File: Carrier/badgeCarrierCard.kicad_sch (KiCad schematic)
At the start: 29 parts, among them J1 USB_C_Receptacle_USB2.0_16P, J2 MDT420M02003, J3 Conn_01x08, J7 Conn_01x10, U11 TPSGM7227YUWQ10G

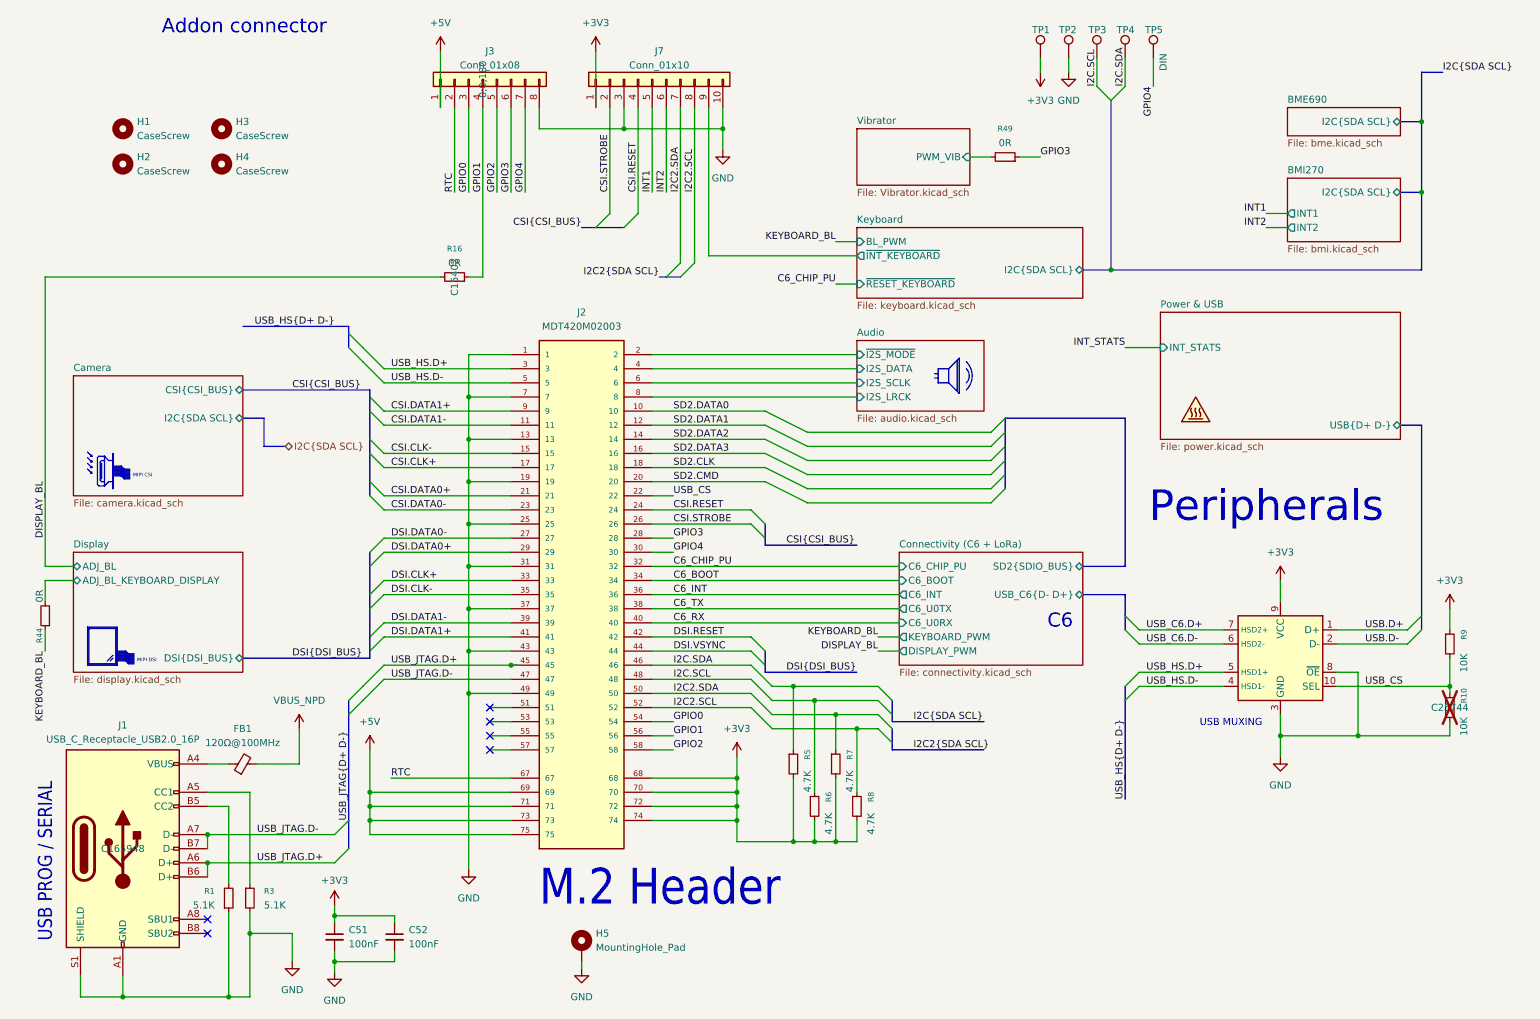
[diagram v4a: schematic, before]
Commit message: feat: add leds and 3dmodels
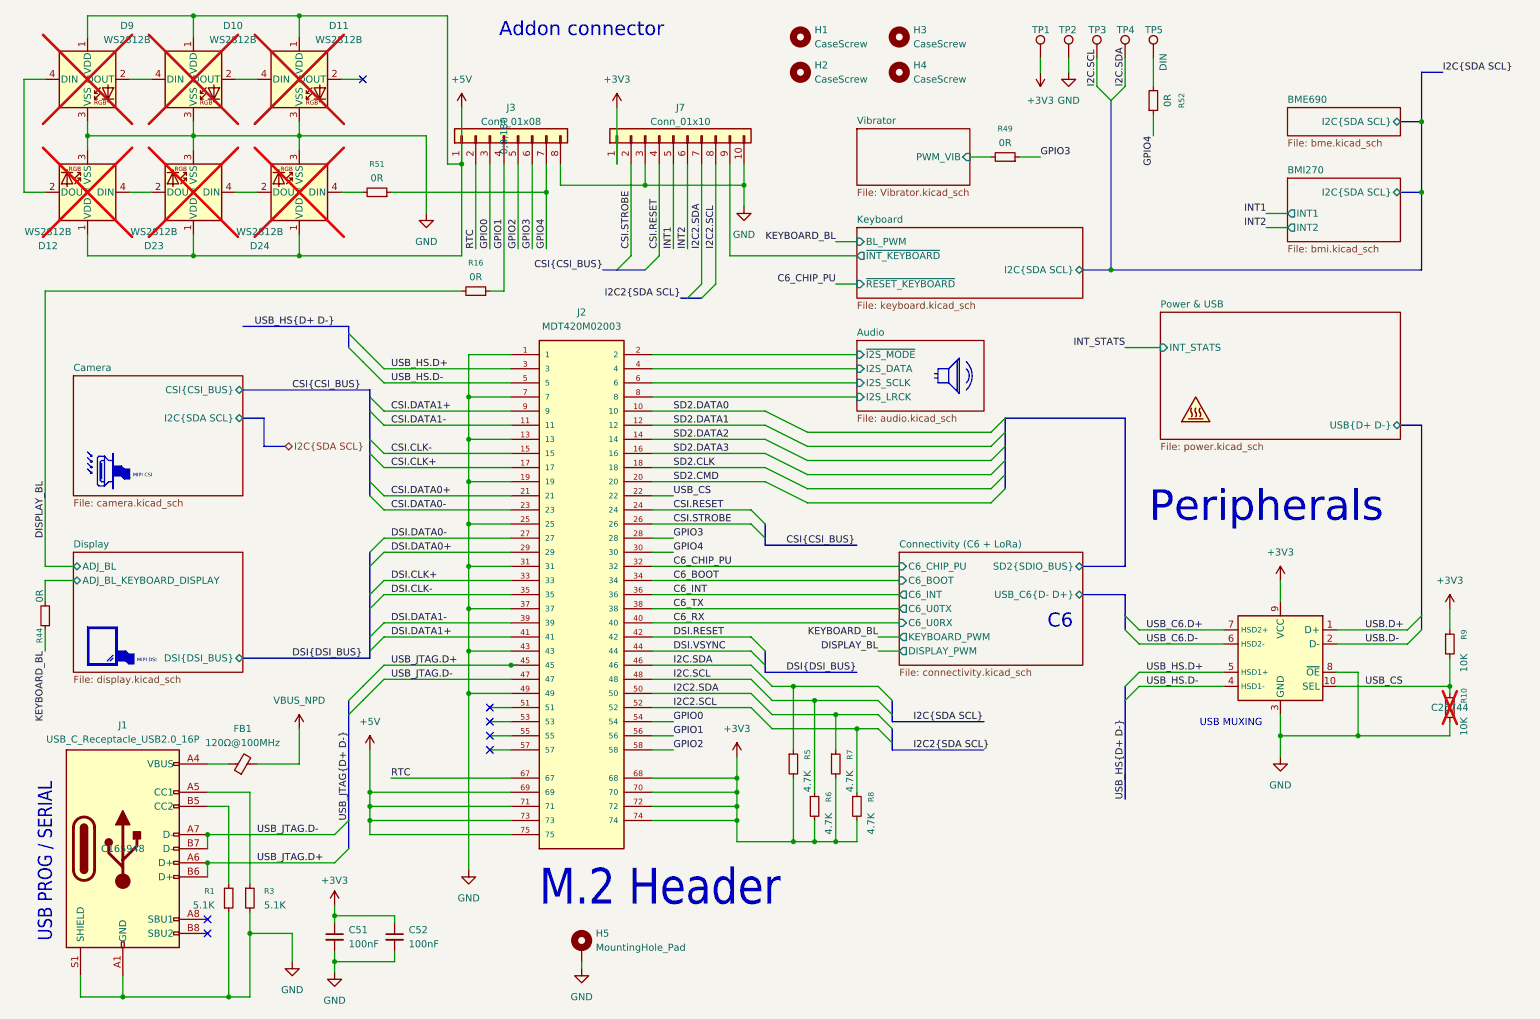
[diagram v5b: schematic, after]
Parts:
- added D10, D11, D12, D23, D24, D9: WS2812B, LED_SMD:LED_WS2812B-Mini_PLCC4_3.5x3.5mm, symbol LED:WS2812B
- added R51, R52: 0R, Resistor_SMD:R_0603_1608Metric, symbol Device:R_Small
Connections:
- net +5V: now also D10.1 (VDD), D11.1 (VDD), D12.1 (VDD), D23.1 (VDD), D24.1 (VDD), D9.1 (VDD)
- net GND: now also D10.3 (VSS), D11.3 (VSS), D12.3 (VSS), D23.3 (VSS), D24.3 (VSS), D9.3 (VSS)
- net GPIO4: now also R51.1, R52.1; no longer TP5.1
- new net: D10.2 (DOUT), D11.4 (DIN)
- new net: D24.4 (DIN), R51.2
- new net: D10.4 (DIN), D9.2 (DOUT)
- new net: D23.4 (DIN), D24.2 (DOUT)
- new net: D12.2 (DOUT), D9.4 (DIN)
- new net: D12.4 (DIN), D23.2 (DOUT)
- new net: R52.2, TP5.1
- no-connect marks 6 -> 7
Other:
- moved on the sheet: H1, H2, H3, H4, J3, J7, R16

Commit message: chore: repo cleanup
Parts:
- R16, R44, R49, R51: now not fitted
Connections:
- net Display/ADJ_BL_KEYBOARD_DISPLAY is gone; now on net KEYBOARD_BL: R44.2
- net DISPLAY_BL: now also R44.1
- net KEYBOARD_BL: no longer R44.1
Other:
- sheet Display ports: added BL_PWM; removed ADJ_BL, ADJ_BL_KEYBOARD_DISPLAY
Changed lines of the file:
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@@
 	)
 	(junction
+		(at 19.05 115.57)
+		(diameter 0)
+		(color 0 0 0 0)
+	)
+	(junction
 		(at 255.27 146.05)
 		(diameter 0)
@@
 		)
 	)
-	(wire
-		(pts
-			(xy 24.13 118.11) (xy 19.05 118.11)
-		)
-		(stroke
-			(width 0)
-			(type default)
-		)
-	)
 	(polyline
 		(pts
@@
 	(wire
 		(pts
+			(xy 19.05 119.38) (xy 19.05 115.57)
+		)
+		(stroke
+			(width 0)
+			(type default)
+		)
+	)
+	(wire
+		(pts
 			(xy 128.27 148.59) (xy 132.08 148.59)
 		)
@@
 	(wire
 		(pts
+			(xy 19.05 124.46) (xy 19.05 128.27)
+		)
+		(stroke
+			(width 0)
+			(type default)
+		)
+	)
+	(wire
+		(pts
 			(xy 121.92 33.02) (xy 121.92 43.18)
 		)
@@
 		)
 	)
-	(wire
-		(pts
-			(xy 19.05 118.11) (xy 19.05 121.92)
-		)
-		(stroke
-			(width 0)
-			(type default)
-		)
-	)
 	(polyline
 		(pts
@@
 		)
 	)
-	(wire
-		(pts
-			(xy 19.05 127) (xy 19.05 130.81)
-		)
-		(stroke
-			(width 0)
-			(type default)
-		)
-	)
 	(bus
 		(pts
@@
 		)
 	)
-	(label "KEYBOARD_BL"
-		(at 19.05 130.81 270)
-		(effects
-			(font
-				(size 1.27 1.27)
-			)
-			(justify right bottom)
-		)
-	)
 	(label "SD2.DATA2"
 		(at 132.08 92.71 0)
@@
 		)
 	)
+	(label "KEYBOARD_BL"
+		(at 19.05 128.27 270)
+		(effects
+			(font
+				(size 1.27 1.27)
+			)
+			(justify right bottom)
+		)
+	)
 	(label "USB_HS{D+ D-}"
 		(at 71.12 72.39 180)
@@
 		(in_bom yes)
 		(on_board yes)
-		(dnp no)
+		(dnp yes)
 		(property "Reference" "R51"
 			(at 78.74 43.18 90)
@@
 	)
 	(symbol
-		(lib_id "Device:R_Small")
-		(at 19.05 124.46 180)
-		(unit 1)
-		(exclude_from_sim no)
-		(in_bom yes)
-		(on_board yes)
-		(dnp no)
-		(property "Reference" "R44"
-			(at 18.034 128.016 90)
-			(effects
-				(font
-					(size 1.016 1.016)
-				)
-			)
-		)
-		(property "Value" "0R"
-			(at 18.034 120.904 90)
-			(effects
-				(font
-					(size 1.27 1.27)
-				)
-			)
-		)
-		(property "Footprint" "Resistor_SMD:R_0603_1608Metric"
-			(at 19.05 124.46 0)
-			(effects
-				(font
-					(size 1.27 1.27)
-				)
-				(hide yes)
-			)
-		)
-		(property "Datasheet" "~"
-			(at 19.05 124.46 0)
-			(effects
-				(font
-					(size 1.27 1.27)
-				)
-				(hide yes)
-			)
-		)
-		(property "Description" "Resistor, small symbol"
-			(at 19.05 124.46 0)
-			(effects
-				(font
-					(size 1.27 1.27)
-				)
-				(hide yes)
-			)
-		)
-		(property "Sim.Device" ""
-			(at 19.05 124.46 0)
-			(effects
-				(font
-					(size 1.27 1.27)
-				)
-			)
-		)
-		(property "LCSC" "C15402"
-			(at 19.05 124.46 0)
-			(effects
-				(font
-					(size 1.27 1.27)
-				)
-				(hide yes)
-			)
-		)
-		(property "DigiKey_Part_Number" ""
-			(at 19.05 124.46 0)
-			(effects
-				(font
-					(size 1.27 1.27)
-				)
-			)
-		)
-		(property "Sim.Pin" ""
-			(at 19.05 124.46 0)
-			(effects
-				(font
-					(size 1.27 1.27)
-				)
-			)
-		)
-		(property "JLCPCB_CORRECTION" ""
-			(at 19.05 124.46 0)
-			(effects
-				(font
-					(size 1.27 1.27)
-				)
-			)
-		)
-		(property "Purchase-URL" ""
-			(at 19.05 124.46 90)
-			(effects
-				(font
-					(size 1.27 1.27)
-				)
-				(hide yes)
-			)
-		)
-		(pin "1"
-		)
-		(pin "2"
-		)
-		(instances
-			(project "badgeCarrierCard"
-				(path "/d0a98fce-b133-4503-8f8a-83b2a1eed591"
-					(reference "R44")
-					(unit 1)
-				)
-			)
-		)
-	)
-	(symbol
 		(lib_id "power:+5V")
 		(at 93.98 33.02 0)
@@
 		(in_bom yes)
 		(on_board yes)
-		(dnp no)
+		(dnp yes)
 		(property "Reference" "R49"
 			(at 191.77 36.83 90)
@@
 		(in_bom yes)
 		(on_board yes)
-		(dnp no)
+		(dnp yes)
 		(property "Reference" "R16"
 			(at 96.52 60.96 90)
@@
 	(symbol
 		(lib_id "Device:R_Small")
+		(at 19.05 121.92 0)
+		(mirror y)
+		(unit 1)
+		(exclude_from_sim no)
+		(in_bom yes)
+		(on_board yes)
+		(dnp yes)
+		(property "Reference" "R44"
+			(at 13.97 121.92 90)
+			(effects
+				(font
+					(size 1.016 1.016)
+				)
+			)
+		)
+		(property "Value" "0R"
+			(at 16.51 121.92 90)
+			(effects
+				(font
+					(size 1.27 1.27)
+				)
+			)
+		)
+		(property "Footprint" "Resistor_SMD:R_0603_1608Metric"
+			(at 19.05 121.92 0)
+			(effects
+				(font
+					(size 1.27 1.27)
+				)
+				(hide yes)
+			)
+		)
+		(property "Datasheet" "~"
+			(at 19.05 121.92 0)
+			(effects
+				(font
+					(size 1.27 1.27)
+				)
+				(hide yes)
+			)
+		)
+		(property "Description" "Resistor, small symbol"
+			(at 19.05 121.92 0)
+			(effects
+				(font
+					(size 1.27 1.27)
+				)
+				(hide yes)
+			)
+		)
+		(property "LCSC" "C15402"
+			(at 19.05 121.92 0)
+			(effects
+				(font
+					(size 1.27 1.27)
+				)
+				(hide yes)
+			)
+		)
+		(property "DigiKey_Part_Number" ""
+			(at 19.05 121.92 0)
+			(effects
+				(font
+					(size 1.27 1.27)
+				)
+			)
+		)
+		(property "Sim.Pin" ""
+			(at 19.05 121.92 0)
+			(effects
+				(font
+					(size 1.27 1.27)
+				)
+			)
+		)
+		(property "JLCPCB_CORRECTION" ""
+			(at 19.05 121.92 0)
+			(effects
+				(font
+					(size 1.27 1.27)
+				)
+			)
+		)
+		(property "Purchase-URL" ""
+			(at 19.05 121.92 90)
+			(effects
+				(font
+					(size 1.27 1.27)
+				)
+				(hide yes)
+			)
+		)
+		(pin "2"
+		)
+		(pin "1"
+		)
+		(instances
+			(project "badgeCarrierCard"
+				(path "/d0a98fce-b133-4503-8f8a-83b2a1eed591"
+					(reference "R44")
+					(unit 1)
+				)
+			)
+		)
+	)
+	(symbol
+		(lib_id "Device:R_Small")
 		(at 52.07 175.26 0)
 		(mirror x)
@@
 			)
 		)
-		(pin "ADJ_BL" bidirectional
-			(at 24.13 115.57 180)
+		(pin "DSI{DSI_BUS}" bidirectional
+			(at 54.61 132.08 0)
 			(effects
 				(font
 					(size 1.27 1.27)
 				)
-				(justify left)
+				(justify right)
 			)
 		)
-		(pin "ADJ_BL_KEYBOARD_DISPLAY" bidirectional
-			(at 24.13 118.11 180)
+		(pin "BL_PWM" input
+			(at 24.13 115.57 180)
 			(effects
 				(font
@@
 			)
 		)
-		(pin "DSI{DSI_BUS}" bidirectional
-			(at 54.61 132.08 0)
-			(effects
-				(font
-					(size 1.27 1.27)
-				)
-				(justify right)
-			)
-		)

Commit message: chore: lib cleanup
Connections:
- net DSI.VSYNC: no longer names the net of J2.44
- no-connect marks 7 -> 8
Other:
- sheet Power & USB ports: added none; removed INT_STATS
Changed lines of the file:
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@@
 	)
 	(junction
-		(at 102.87 133.35)
-		(diameter 0)
-		(color 0 0 0 0)
-	)
-	(junction
 		(at 45.72 16.51)
 		(diameter 0)
@@
 	)
 	(no_connect
+		(at 132.08 130.81)
+	)
+	(no_connect
 		(at 99.06 146.05)
 	)
@@
 	)
 	(bus_entry
-		(at 148.59 133.35)
-		(size -2.54 -2.54)
-		(stroke
-			(width 0)
-			(type default)
-		)
-	)
-	(bus_entry
 		(at 77.47 85.09)
 		(size 2.54 2.54)
@@
 		)
 	)
-	(wire
-		(pts
-			(xy 104.14 133.35) (xy 102.87 133.35)
-		)
-		(stroke
-			(width 0)
-			(type default)
-		)
-	)
 	(bus
 		(pts
@@
 		)
 	)
-	(bus
-		(pts
-			(xy 148.59 133.35) (xy 148.59 134.62)
-		)
-		(stroke
-			(width 0)
-			(type default)
-		)
-	)
 	(polyline
 		(pts
@@
 	(wire
 		(pts
-			(xy 213.36 76.2) (xy 219.71 76.2)
-		)
-		(stroke
-			(width 0)
-			(type default)
-		)
-	)
-	(wire
-		(pts
 			(xy 95.25 130.81) (xy 102.87 130.81)
 		)
@@
 	(wire
 		(pts
+			(xy 128.27 130.81) (xy 132.08 130.81)
+		)
+		(stroke
+			(width 0)
+			(type default)
+		)
+	)
+	(wire
+		(pts
 			(xy 99.06 66.04) (xy 101.6 66.04)
 		)
@@
 		)
 	)
-	(wire
-		(pts
-			(xy 128.27 130.81) (xy 146.05 130.81)
-		)
-		(stroke
-			(width 0)
-			(type default)
-		)
-	)
 	(polyline
 		(pts
@@
 	(bus
 		(pts
-			(xy 148.59 130.81) (xy 148.59 133.35)
+			(xy 148.59 130.81) (xy 148.59 134.62)
 		)
 		(stroke
@@
 		)
 	)
-	(label "INT_STATS"
-		(at 213.36 76.2 180)
-		(effects
-			(font
-				(size 1.27 1.27)
-			)
-			(justify right bottom)
-		)
-	)
 	(label "I2C.SCL"
 		(at 208.28 29.21 90)
@@
 		)
 	)
-	(label "DSI.VSYNC"
-		(at 132.08 130.81 0)
-		(effects
-			(font
-				(size 1.27 1.27)
-			)
-			(justify left bottom)
-		)
-	)
 	(label "KEYBOARD_BL"
 		(at 168.91 128.27 180)
@@
 	(symbol
 		(lib_id "Graphic:SYM_Hot_Small")
-		(at 226.06 87.63 0)
+		(at 240.03 87.63 0)
 		(unit 1)
 		(exclude_from_sim yes)
@@
 		(fields_autoplaced yes)
 		(property "Reference" "#SYM1"
-			(at 226.06 84.074 0)
+			(at 240.03 84.074 0)
 			(effects
 				(font
@@
 		)
 		(property "Value" "SYM_Hot_Small"
-			(at 226.06 90.805 0)
+			(at 240.03 90.805 0)
 			(effects
 				(font
@@
 		)
 		(property "Footprint" ""
-			(at 226.06 92.075 0)
+			(at 240.03 92.075 0)
 			(effects
 				(font
@@
 		)
 		(property "Datasheet" "~"
-			(at 226.822 92.71 0)
+			(at 240.792 92.71 0)
 			(effects
 				(font
@@
 		)
 		(property "Description" "Hot surface warning symbol, small"
-			(at 226.06 87.63 0)
+			(at 240.03 87.63 0)
 			(effects
 				(font
@@
 	)
 	(sheet
-		(at 219.71 69.85)
-		(size 43.18 22.86)
+		(at 234.95 81.28)
+		(size 27.94 11.43)
 		(exclude_from_sim no)
 		(in_bom yes)
@@
 		)
 		(property "Sheetname" "Power & USB"
-			(at 219.71 69.1384 0)
+			(at 234.95 80.5684 0)
 			(effects
 				(font
@@
 		)
 		(property "Sheetfile" "power.kicad_sch"
-			(at 219.71 93.2946 0)
+			(at 234.95 93.2946 0)
 			(effects
 				(font
@@
 			)
 		)
-		(pin "INT_STATS" input
-			(at 219.71 76.2 180)
-			(effects
-				(font
-					(size 1.27 1.27)
-				)
-				(justify left)
-			)
-		)

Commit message: fix: last minute resistor changes
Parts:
- added R45: 0R, Resistor_SMD:R_0603_1608Metric, symbol Device:R_Small
- added R53: 0R, Resistor_SMD:R_0402_1005Metric, symbol Device:R_Small
- R52: now not fitted
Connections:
- net GPIO3: now also R53.1; no longer J3.6 (Pin_6)
- net GPIO4: now also R45.1; no longer J3.7 (Pin_7)
- new net: J3.7 (Pin_7), R45.2
- new net: J3.6 (Pin_6), R53.2
